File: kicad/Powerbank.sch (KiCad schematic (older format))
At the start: 0 parts

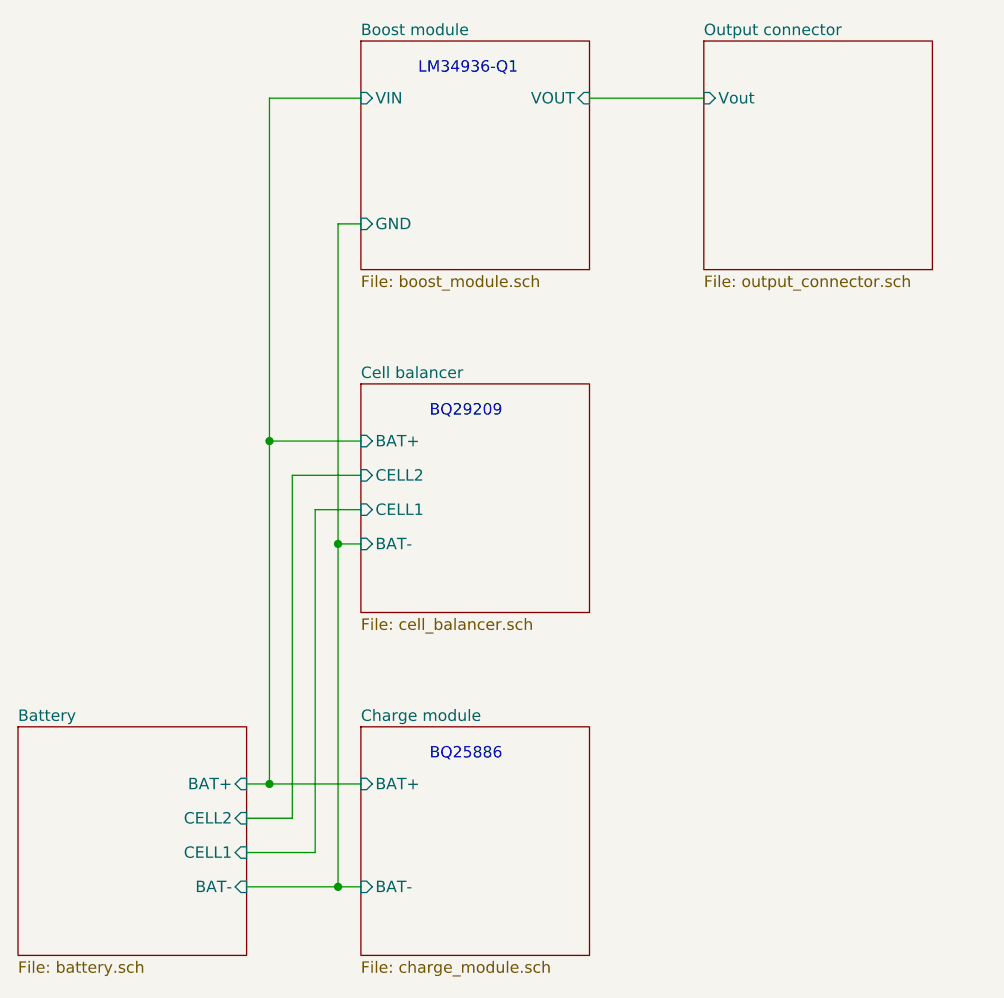
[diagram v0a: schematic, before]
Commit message: Updated schematic
Made some error with first rev, the found error are now corrected.
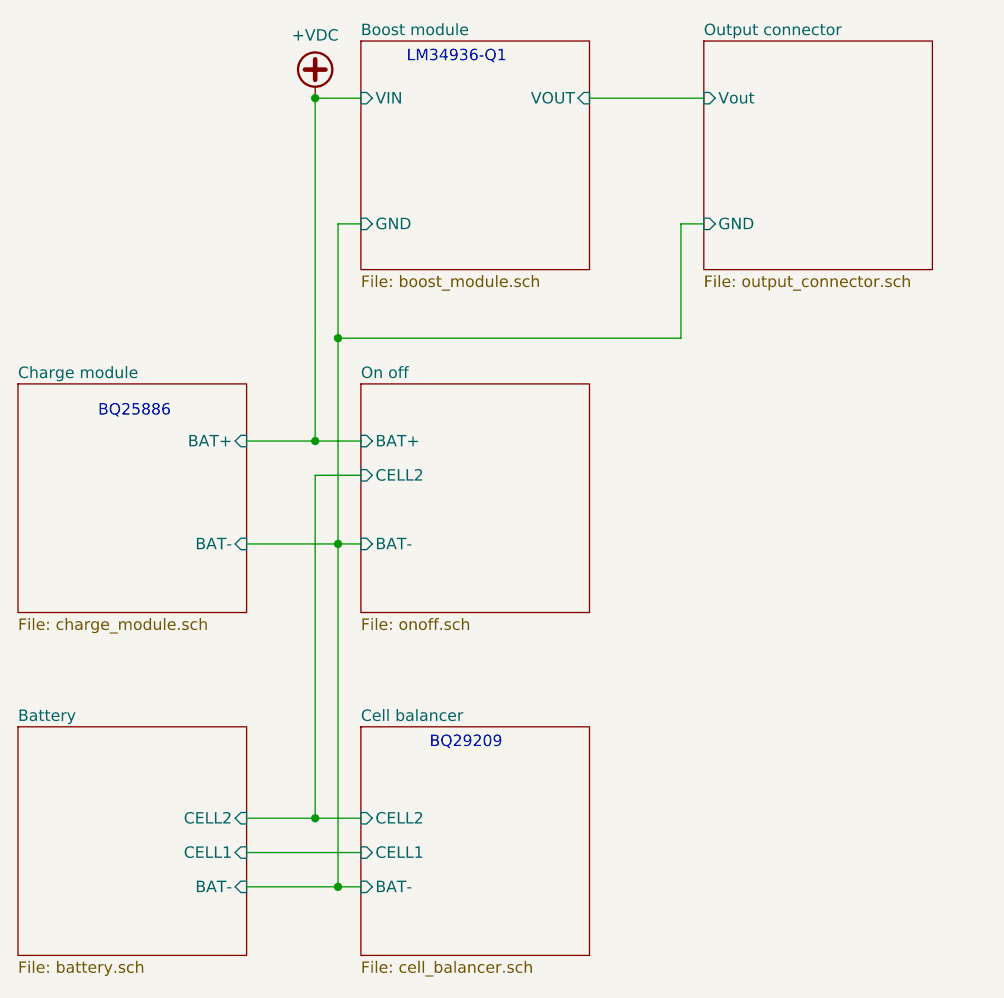
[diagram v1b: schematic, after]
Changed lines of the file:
@@
 $Descr A4 11693 8268
 encoding utf-8
-Sheet 1 6
+Sheet 1 7
 Title "USB-C PD controller with 4S battery charger"
 Date "2020-01-11"
@@
 F0 "Battery" 50
 F1 "battery.sch" 50
-F2 "BAT+" I R 4000 5250 50
-F3 "BAT-" I R 4000 5700 50
-F4 "CELL2" I R 4000 5400 50
-F5 "CELL1" I R 4000 5550 50
+F2 "BAT-" I R 4000 5700 50
+F3 "CELL2" I R 4000 5400 50
+F4 "CELL1" I R 4000 5550 50
 $EndSheet
 $Sheet
-S 4500 3500 1000 1000
+S 4500 5000 1000 1000
 U 5FAE55EF
 F0 "Cell balancer" 50
 F1 "cell_balancer.sch" 50
-F2 "BAT+" I L 4500 3750 50
-F3 "BAT-" I L 4500 4200 50
-F4 "CELL1" I L 4500 4050 50
-F5 "CELL2" I L 4500 3900 50
+F2 "BAT-" I L 4500 5700 50
+F3 "CELL1" I L 4500 5550 50
+F4 "CELL2" I L 4500 5400 50
 $EndSheet
-Wire Wire Line
-	4000 5550 4300 5550
-Wire Wire Line
-	4000 5250 4100 5250
-$Sheet
-S 4500 5000 1000 1000
-U 5FAEE37B
-F0 "Charge module" 50
-F1 "charge_module.sch" 50
-F2 "BAT+" I L 4500 5250 50
-F3 "BAT-" I L 4500 5700 50
-$EndSheet
-Wire Wire Line
-	4500 4200 4400 4200
-Wire Wire Line
-	4400 4200 4400 5700
-Wire Wire Line
-	4300 5550 4300 4050
-Wire Wire Line
-	4300 4050 4500 4050
-Wire Wire Line
-	4500 3900 4200 3900
-Wire Wire Line
-	4200 3900 4200 5400
-Wire Wire Line
-	4100 3750 4500 3750
-Connection ~ 4400 5700
-Wire Wire Line
-	4400 5700 4000 5700
-Wire Wire Line
-	4400 5700 4500 5700
-Wire Wire Line
-	4000 5400 4200 5400
-Wire Wire Line
-	4100 3750 4100 5250
-Connection ~ 4100 5250
-Wire Wire Line
-	4100 5250 4500 5250
-Connection ~ 4100 3750
-Text Notes 4800 5150 0    50   ~ 0
+Text Notes 3350 3650 0    50   ~ 0
 BQ25886
-Text Notes 4750 2150 0    50   ~ 0
+Text Notes 4700 2100 0    50   ~ 0
 LM34936-Q1
 Wire Wire Line
-	4100 2250 4500 2250
-Wire Wire Line
-	4100 2250 4100 3750
-Wire Wire Line
-	4400 4200 4400 2800
+	4300 2250 4500 2250
 Wire Wire Line
 	4400 2800 4500 2800
-Connection ~ 4400 4200
 $Sheet
 S 6000 2000 1000 1000
@@
 F1 "output_connector.sch" 50
 F2 "Vout" I L 6000 2250 50
+F3 "GND" I L 6000 2800 50
 $EndSheet
 Wire Wire Line
 	6000 2250 5500 2250
-Text Notes 4800 3650 0    50   ~ 0
+Text Notes 4800 5100 0    50   ~ 0
 BQ29209
+Wire Wire Line
+	4000 5700 4400 5700
+Wire Wire Line
+	4000 5400 4300 5400
+Wire Wire Line
+	4000 5550 4500 5550
+$Sheet
+S 4500 3500 1000 1000
+U 5FC1217D
+F0 "On off " 50
+F1 "onoff.sch" 50
+F2 "BAT+" I L 4500 3750 50
+F3 "CELL2" I L 4500 3900 50
+F4 "BAT-" I L 4500 4200 50
+$EndSheet
+Wire Wire Line
+	4500 4200 4400 4200
+Connection ~ 4400 4200
+Wire Wire Line
+	4500 3900 4300 3900
+Wire Wire Line
+	4300 3900 4300 5400
+Connection ~ 4300 5400
+Wire Wire Line
+	4300 5400 4500 5400
+Wire Wire Line
+	4400 4200 4400 5700
+Connection ~ 4400 5700
+Wire Wire Line
+	4400 5700 4500 5700
+Wire Wire Line
+	4500 3750 4300 3750
+Wire Wire Line
+	4400 2800 4400 3300
+Wire Wire Line
+	4300 2250 4300 3750
+Wire Wire Line
+	4000 3750 4300 3750
+Connection ~ 4300 3750
+Wire Wire Line
+	4000 4200 4400 4200
+Wire Wire Line
+	6000 2800 5900 2800
+Wire Wire Line
+	5900 2800 5900 3300
+Wire Wire Line
+	5900 3300 4400 3300
+Connection ~ 4400 3300
+Wire Wire Line
+	4400 3300 4400 4200
+$Comp
+L power:+VDC #PWR0129
+U 1 1 5FC58AEF
+P 4300 2250
+F 0 "#PWR0129" H 4300 2150 50  0001 C CNN
+F 1 "+VDC" H 4300 2525 50  0000 C CNN
+F 2 "" H 4300 2250 50  0001 C CNN
+F 3 "" H 4300 2250 50  0001 C CNN
+	1    4300 2250
+	1    0    0    -1
+$EndComp
+Connection ~ 4300 2250
+$Sheet
+S 3000 3500 1000 1000
+U 5FAEE37B
+F0 "Charge module" 50
+F1 "charge_module.sch" 50
+F2 "BAT+" I R 4000 3750 50
+F3 "BAT-" I R 4000 4200 50
+$EndSheet
 $EndSCHEMATC
